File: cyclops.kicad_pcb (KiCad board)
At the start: 2 copper layers, 311.4 x 93.5 mm, 160 parts, among them J1 USB_mini_micro_B, J2 MISO, K1 ESC, K10 KEYSW, K11 KEYSW, K12 KEYSW, K13 KEYSW, K14 backspace, K15 tab, K16 KEYSW, K17 KEYSW, K18 KEYSW, K19 KEYSW, K2 1, K20 KEYSW, K21 KEYSW, K22 KEYSW, K23 KEYSW, K24 KEYSW, K25 KEYSW, K26 KEYSW, K27 KEYSW, K28 Lock, K29 KEYSW, K3 KEYSW, K30 KEYSW, K31 KEYSW, K32 KEYSW, K33 KEYSW, K34 KEYSW, K35 KEYSW, K36 KEYSW, K37 KEYSW, K38 KEYSW, K39 KEYSW, K4 KEYSW, K40 KEYSW, K41 Shift, K42 KEYSW, K43 KEYSW, K44 KEYSW, K45 KEYSW, K46 KEYSW, K47 KEYSW, K48 KEYSW, K49 KEYSW, K5 KEYSW, K50 KEYSW, K51 KEYSW, K52 KEYSW, K53 Shift, K54 Ctrl, K55 alt, K56 opt, K57 space, K58 cmd, K59 alt, K6 KEYSW, K60 ctrl, K61 enter, K62 backspace, K63 KEYSW, K64 Shift, K64-2 Shift, K65 Shift, K66 Shift, K67 Shift, K7 KEYSW, K8 KEYSW, K9 KEYSW, SW1 SW_Push, U1 ATMEGA32U4, X1 16mhz

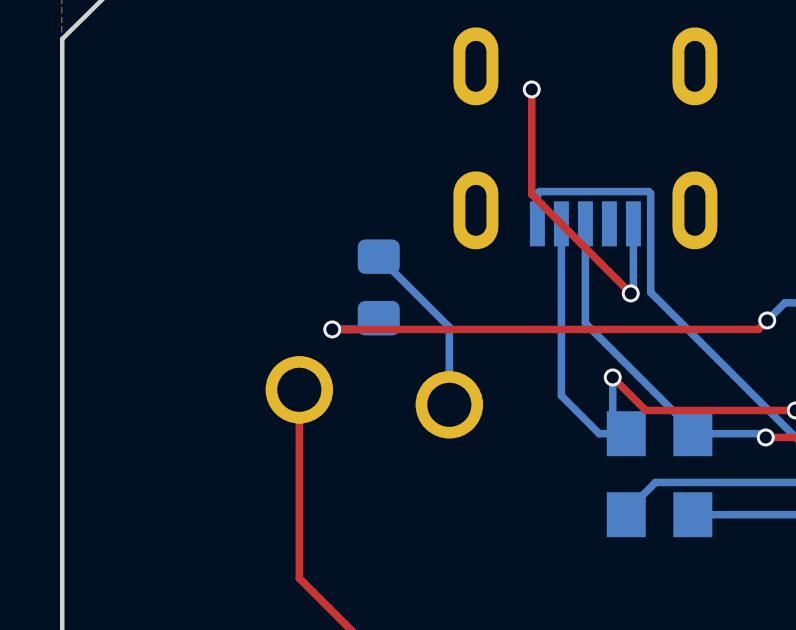
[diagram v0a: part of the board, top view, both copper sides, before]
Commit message: minor adjustment of D1
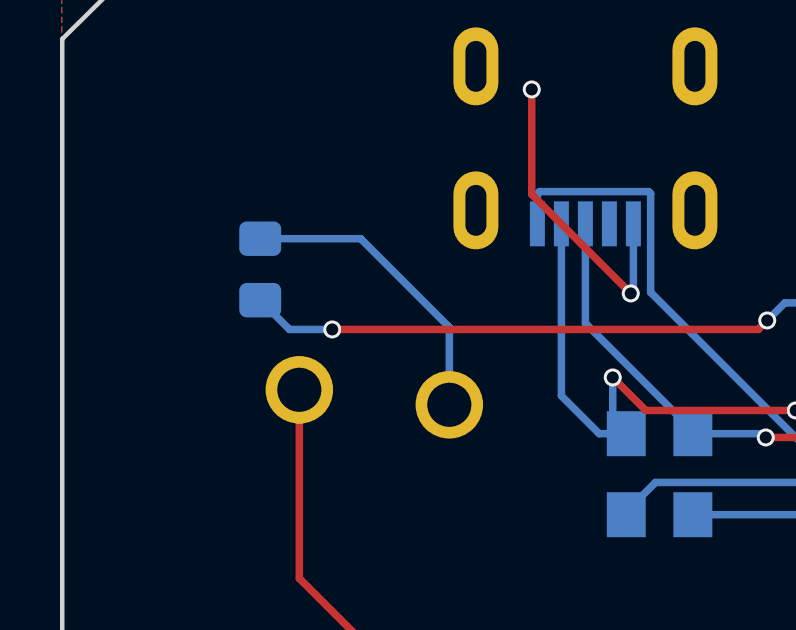
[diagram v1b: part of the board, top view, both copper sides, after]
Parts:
- moved D1 4.00 mm to (75.8, 107.1)
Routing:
- net Net-(D1-Pad2): track 5.91 -> 10.1 mm
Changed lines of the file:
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@@
   )
   (module Diode_SMD:D_0805_2012Metric_Pad1.15x1.40mm_HandSolder (layer B.Cu)
-    (at 79.7 107.7 90)
+    (at 75.75 107.1 90)
     (descr "Diode SMD 0805 (2012 Metric), square (rectangular) end terminal, IPC_7351 nominal, (Body size source: https://docs.google.com/spreadsheets/d/1BsfQQcO9C6DZCsRaXUlFlo91Tg2WpOkGARC1WS5S8t0/edit?usp=sharing), generated with kicad-footprint-generator")
     (tags "diode handsolder")
@@
   (via (at 78.15 109.1) (size 0.6) (drill 0.4) (layers F.Cu B.Cu) (net 4))
   (segment (start 92.35 109.1) (end 78.15 109.1) (width 0.25) (layer F.Cu) (net 4))
-  (segment (start 78.15 109.1) (end 78.90459 109.1) (width 0.25) (layer B.Cu) (net 4))
-  (segment (start 79.325 109.1) (end 79.7 108.725) (width 0.25) (layer B.Cu) (net 4) (status 30))
-  (segment (start 78.15 109.1) (end 79.325 109.1) (width 0.25) (layer B.Cu) (net 4) (status 20))
   (segment (start 363.175 108.275) (end 367.65 108.275) (width 0.25) (layer B.Cu) (net 4) (status 20))
   (segment (start 344.15 114.7) (end 356.75 114.7) (width 0.25) (layer B.Cu) (net 4))
   (segment (start 356.75 114.7) (end 363.175 108.275) (width 0.25) (layer B.Cu) (net 4))
-  (segment (start 82.0528 109.0278) (end 82.0528 111.6118) (width 0.25) (layer B.Cu) (net 5) (status 20))
-  (segment (start 79.7 106.675) (end 82.0528 109.0278) (width 0.25) (layer B.Cu) (net 5) (status 10))
+  (segment (start 76.725 109.1) (end 78.15 109.1) (width 0.25) (layer B.Cu) (net 4))
+  (segment (start 75.75 108.125) (end 76.725 109.1) (width 0.25) (layer B.Cu) (net 4))
+  (segment (start 82.0528 111.6118) (end 82.0528 109.0278) (width 0.25) (layer B.Cu) (net 5))
+  (segment (start 82.0528 109.0278) (end 79.1 106.075) (width 0.25) (layer B.Cu) (net 5))
+  (segment (start 79.1 106.075) (end 75.75 106.075) (width 0.25) (layer B.Cu) (net 5))
   (segment (start 105.3731 102.6111) (end 103.4904 102.6111) (width 0.25) (layer B.Cu) (net 6) (status 20))
   (segment (start 107.95 105.188) (end 105.3731 102.6111) (width 0.25) (layer B.Cu) (net 6))

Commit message: Updated layout of decoupling caps
generated new gerbers
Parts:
- moved C8 0.75 mm to (172.2, 187.6), turned to 180 degrees
- moved C2 0.55 mm to (180.8, 187.6), turned to 0 degrees
- moved C5 0.50 mm to (176.5, 187.6), turned to 0 degrees
- moved C3 0.45 mm to (167.1, 167.7), turned to 180 degrees
- moved R4 0.39 mm to (176.8, 167.7), turned to 180 degrees
- moved C4 0.22 mm to (167.9, 187.6), turned to 0 degrees
- turned C1 to 0 degrees
- turned R3 to 0 degrees
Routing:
- net GND: track 80.0 -> 95.7 mm, vias 8 -> 19
- net VCC: track 449.0 -> 457.0 mm
- net /RESET: track 179.2 -> 181.7 mm
- net /COL3: track 104.5 -> 106.7 mm
- net Net-(R4-Pad1): track 4.49 -> 6.15 mm
- net /COL8: track 143.0 -> 144.7 mm
- net /COL9: track 160.9 -> 162.2 mm
- net Net-(C8-Pad2): track 5.00 -> 3.74 mm
- net /COL4: track 94.0 -> 95.0 mm
- net /ROW3: track 285.8 -> 286.4 mm
